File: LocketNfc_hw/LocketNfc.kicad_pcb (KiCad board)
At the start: 2 copper layers, 75.2 x 67.4 mm, 168 parts, among them M1 MOTOR_NO_CONTACTS, Q1 IRLML6401, Q2 IRLML6401, Q3 LED_RGB 5050, Q4 IRLML2030, SW1 SWITCH, SW2 IT1198, SW3 IT1198, SW4 IT1198

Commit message: Placement in progress
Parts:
- removed C123: 3.3pF, Capacitors:CAP_0402
- removed L123, L124: 12nH, Inductors:IND_0402
- removed TP2: TESTPOINT, PCB:TESTPOINT_1MM
- added C24: *, Capacitors:CAP_0402, B.Cu at (125.2, 85.7)
- added C59: 10u, Capacitors:CAP_0603_Silks, B.Cu at (195.0, 121.2)
- added C60: 10u, Capacitors:CAP_0603_Silks, B.Cu at (195.0, 118.4)
- added R29: 56k, Resistors:RES_0603, B.Cu at (185.2, 132.1)
- added R30: 56k, Resistors:RES_0603, B.Cu at (189.4, 132.1)
- added R31: 10k, Resistors:RES_0603, B.Cu at (190.9, 121.2)
- added R32: 10k, Resistors:RES_0603, B.Cu at (190.9, 118.4)
- ANT1: footprint Antennas:Locket5 -> Antennas:LocketNFC_inverted; moved to B.Cu
- C125: value 12pF -> 100pF; footprint Capacitors:CAP_0603 -> Capacitors:CAP_0402
- RP3, RP4, XL11, XL12: moved to F.Cu
- moved DD3 129.0 mm to (135.6, 83.8)
- moved C125 115.9 mm to (127.0, 84.0), turned to 0 degrees
- moved C121 113.1 mm to (129.6, 84.0), turned to 90 degrees
- moved L132 112.4 mm to (128.0, 85.2), turned to 0 degrees
- moved ANT1 112.0 mm to (124.1, 100.0), turned to 90 degrees
- moved C122 111.9 mm to (128.0, 82.8)
- moved C52 111.6 mm to (131.5, 86.8), turned to -90 degrees
- moved C51 110.2 mm to (131.5, 81.2), turned to 90 degrees
- moved L6 107.6 mm to (125.0, 84.0), turned to 0 degrees
- moved C49 104.5 mm to (133.5, 78.7), turned to 90 degrees
- moved XTAL3 102.4 mm to (135.5, 90.4)
- moved C28 95.4 mm to (135.8, 92.9)
- moved L131 91.1 mm to (131.2, 84.6), turned to 0 degrees
- moved XL11 90.2 mm to (135.3, 128.0), turned to 90 degrees
- moved XL12 90.0 mm to (132.4, 128.0), turned to 90 degrees
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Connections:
- C125 pad 2: /ANT0 -> /RF5
- DD1 pad 1: /AU_MCLK -> unconnected-(DD1-Pad1)
- DD1 pad 67: /AU_MCLK -> unconnected-(DD1-Pad67)
- MDL1 pad 10: /AU_MCLK -> /AU_LRCK
- MDL1 pad 11: /AU_LRCK -> /AU_BITCK
- MDL1 pad 12: /AU_BITCK -> /AU_SDA
- MDL1 pad 24: GND -> Net-(MDL1-Pad24)
- MDL1 pad 8: /AU_SDA -> /ESP_AUX
- MDL1 pad 9: /ESP_AUX -> unconnected-(MDL1-Pad9)
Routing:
- net VCC: track 0.00 -> 17.6 mm
- net +PwrMCU: track 0.00 -> 16.2 mm
- net GND: track 8.99 -> 20.3 mm
- net Net-(C1-Pad1): track 0.00 -> 10.4 mm
- net Net-(C15-Pad2): track 0.00 -> 4.74 mm
- net /RF3: track 0.00 -> 3.80 mm
- net /RF4: track 0.00 -> 3.75 mm
- net Net-(DD1-Pad13): track 0.00 -> 3.04 mm
- net /RF5: track 0.00 -> 2.50 mm
- net Net-(DD3-Pad17): track 0.00 -> 2.35 mm
- net Net-(C30-Pad2): track 0.00 -> 2.09 mm
- net /RF2: track 0.00 -> 2.04 mm
- net /RF1: track 0.00 -> 2.04 mm
- net Net-(C2-Pad1): track 0.00 -> 1.95 mm
- net /CC_MISO: track 0.00 -> 1.72 mm
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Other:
- copper layers 2 -> 4

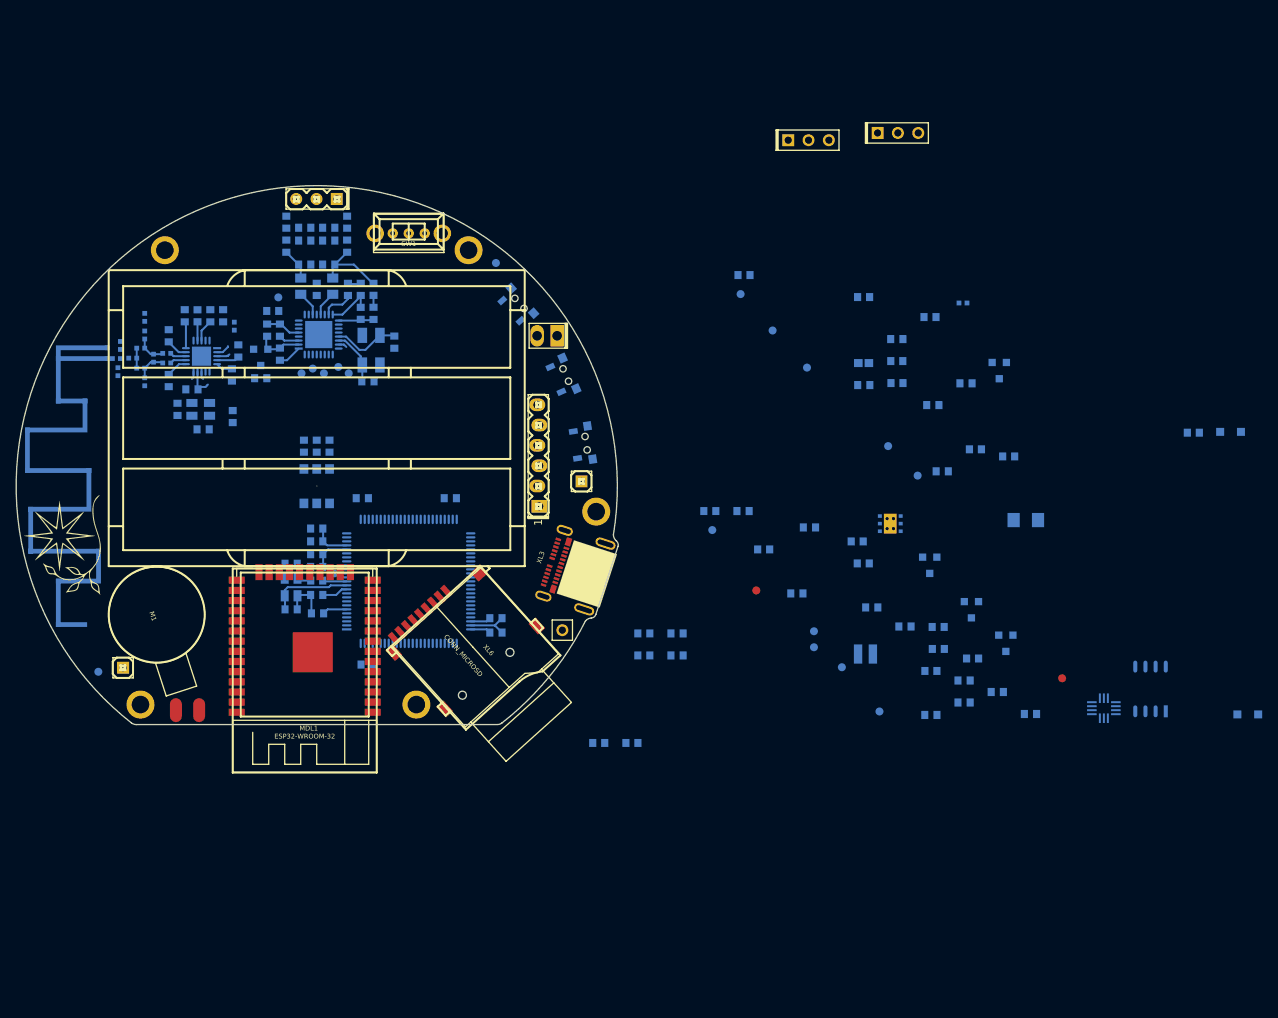
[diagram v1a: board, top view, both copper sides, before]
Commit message: Main PCB sent to factory
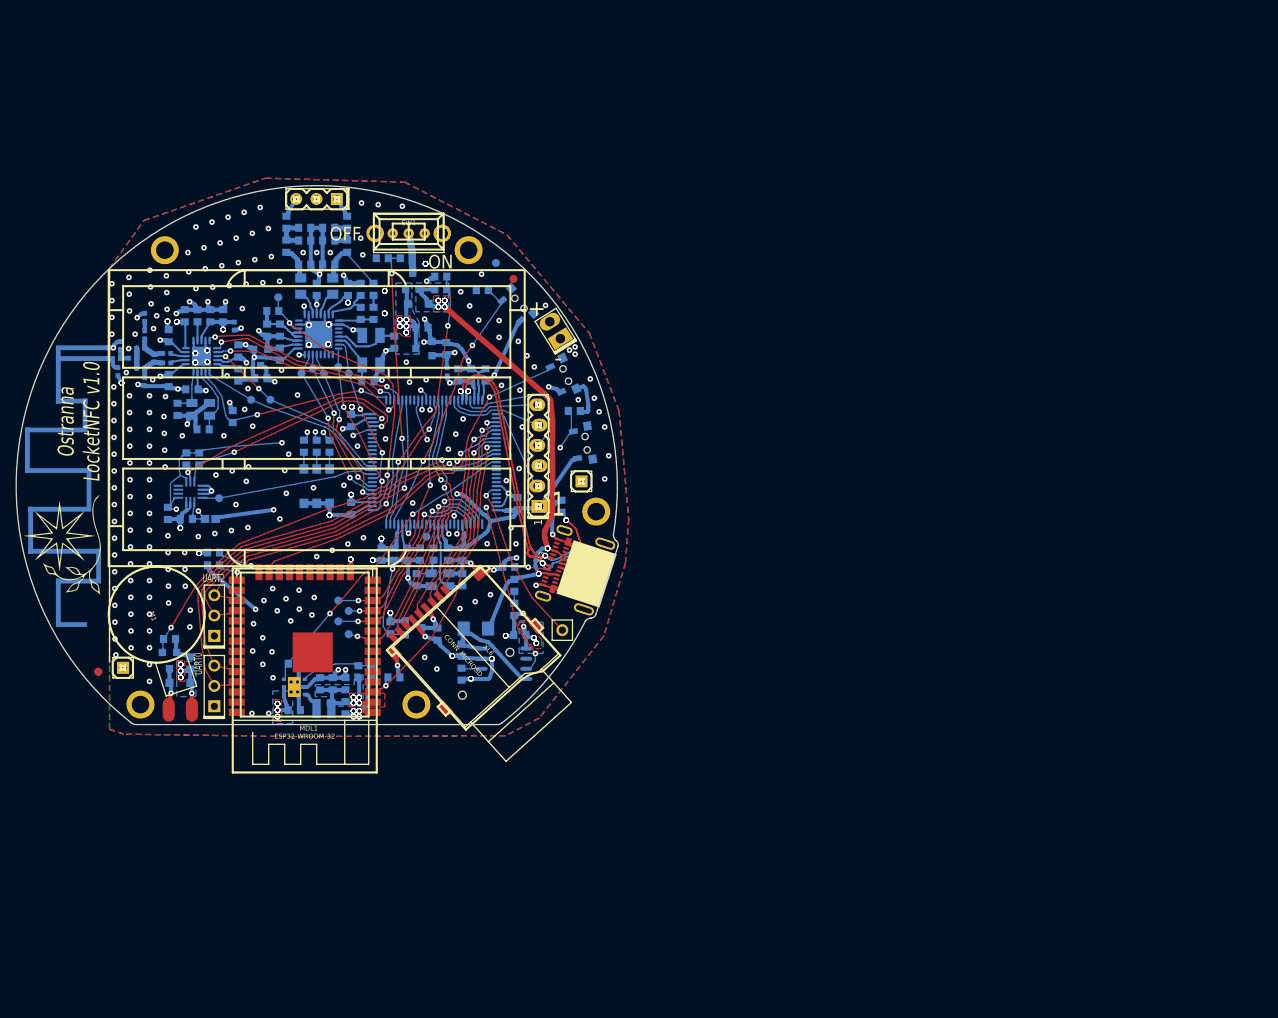
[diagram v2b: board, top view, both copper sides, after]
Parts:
- removed C59, C60: 10u, Capacitors:CAP_0603_Silks
- removed TP14, TP15, TP16: TESTPOINT, PCB:TESTPOINT_1MM
- R23: value 1k -> 68R
- R24: value 1k -> 330R
- R25: value 1k -> 150R
- moved D2 133.5 mm to (132.9, 124.6)
- moved RP3 120.5 mm to (122.7, 123.2)
- moved DD4 117.4 mm to (134.2, 100.7)
- moved XL4 109.6 mm to (137.2, 127.5), turned to 90 degrees
- moved D1 102.8 mm to (162.7, 77.2), turned to 0 degrees
- moved C56 98.2 mm to (134.2, 122.1), turned to -90 degrees
- moved R26 97.0 mm to (135.3, 96.6), turned to 90 degrees
- moved Q4 95.8 mm to (131.6, 121.8)
- moved XL5 94.8 mm to (137.2, 118.7), turned to 90 degrees
- moved C25 87.9 mm to (147.2, 128.0), turned to 0 degrees
- moved R27 87.0 mm to (133.7, 96.6), turned to 90 degrees
- moved R28 86.8 mm to (131.6, 119.1), turned to 0 degrees
- moved C47 85.7 mm to (153.6, 124.7), turned to 90 degrees
- moved F1 84.0 mm to (136.7, 104.1)
- moved TP17 83.9 mm to (137.8, 101.5)
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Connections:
- net /RF5 renamed /ANT0
- Q3 pad 1: GND -> Net-(Q3-Pad1)
- Q3 pad 2: GND -> Net-(Q3-Pad2)
- Q3 pad 3: GND -> Net-(Q3-Pad3)
- Q3 pad 4: Net-(Q3-Pad4) -> GND
- Q3 pad 5: Net-(Q3-Pad5) -> GND
- Q3 pad 6: Net-(Q3-Pad6) -> GND
- R23 pad 2: Net-(Q3-Pad4) -> Net-(Q3-Pad1)
- R24 pad 2: Net-(Q3-Pad5) -> Net-(Q3-Pad2)
- R25 pad 2: Net-(Q3-Pad6) -> Net-(Q3-Pad3)
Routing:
- net GND: track 20.3 -> 484.3 mm, vias 0 -> 370
- net +PwrMCU: track 16.2 -> 180.7 mm, vias 0 -> 25
- net +PwrUnst: track 0.00 -> 100.6 mm, vias 0 -> 57
- net /USB_D+: track 0.00 -> 73.8 mm, vias 0 -> 15
- net +BATT: track 0.00 -> 73.2 mm, vias 0 -> 11
- net /USB_D-: track 0.00 -> 67.3 mm, vias 0 -> 15
- net /+5V_USB: track 0.00 -> 63.7 mm, vias 0 -> 30
- net /ESP_TX0_MCU_RX: track 0.00 -> 58.4 mm, vias 0 -> 1
- net /ESP_RX0_MCU_TX: track 0.00 -> 54.5 mm, vias 0 -> 1
- net /Vibro_CTRL: track 0.00 -> 49.7 mm, vias 0 -> 2
- net /ESP_TX2_MCU_RX: track 0.00 -> 45.9 mm, vias 0 -> 1
- net /PWR_ACG: track 0.00 -> 43.7 mm, vias 0 -> 4
- net /ESP_RX2_MCU_TX: track 0.00 -> 41.2 mm, vias 0 -> 1
- net /ESP_GPIO0: track 0.00 -> 40.3 mm, vias 0 -> 2
- net /+PWR_ESP: track 0.00 -> 39.9 mm, vias 0 -> 21
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- added copper zone on B.Cu, net +BATT
- added copper zone on F.Cu, net +BATT
- added copper zone on In1.Cu, net +BATT
- added copper zone on In2.Cu, net +BATT
- added copper zone on B.Cu, net +PwrUnst
- added copper zone on F.Cu, net +PwrUnst
- added copper zone on In1.Cu, net +PwrUnst
- added copper zone on In2.Cu, net +PwrUnst
- added copper zone on B.Cu, net /+5V_USB
- added copper zone on F.Cu, net /+5V_USB
- added copper zone on In1.Cu, net /+5V_USB
- added copper zone on In2.Cu, net /+5V_USB
- added copper zone on B.Cu, net /+PWR_ESP
- added copper zone on F.Cu, net /+PWR_ESP
- added copper zone on In1.Cu, net /+PWR_ESP
- added copper zone on In2.Cu, net /+PWR_ESP
- added copper zone on B.Cu, net GND
- added copper zone on F.Cu, net GND
- added copper zone on In1.Cu, net GND
- added copper zone on In2.Cu, net GND
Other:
- outline, holes or cut-outs redrawn
- board text added: "+"
- board text added: "-"
- board text added: "1"
- board text added: "ACG"
- board text added: "AUX"
- board text added: "BCK"
- board text added: "Charger"
- board text added: "DBG"
- board text added: "GDO0"
- board text added: "GDO2"
- board text added: "GND"
- board text added: "IRQ"
- board text added: "LRCK"
- board text added: "MISO"
- board text added: "MOSI"
- board text added: "NSS"
- board text added: "OFF"
- board text added: "ON"
- board text added: "Ostranna LocketNFC v1.0"
- board text added: "RX0"
- board text added: "RX2"
- board text added: "SCK"
- board text added: "SDA"
- board text added: "Solder to power ACG always"
- board text added: "TX0"
- board text added: "TX2"
- board text added: "UART0"
- board text added: "UART2"
- board text added: "Vibro"

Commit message: Connects
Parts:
- turned Q3 to -90 degrees
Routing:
- net Net-(Q3-Pad3): track 0.00 -> 2.10 mm
- net GND: track 484.3 -> 482.2 mm
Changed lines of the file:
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@@
     )
   )
-  (footprint "LEDs:LED_5050" locked (layer "B.Cu")
-    (at 150 100 90)
+  (footprint "LEDs:LED_5050" (layer "B.Cu")
+    (at 150 100 -90)
     (property "Price" "7")
     (property "Sheetfile" "LocketNfc.kicad_sch")
@@
     (fp_line (start -2.49936 2.49936) (end 2.49936 2.49936) (layer "B.SilkS") (width 0.14986))
     (fp_circle (center 0 0) (end 0 -2.19964) (layer "B.SilkS") (width 0.14986) (fill none))
-    (pad "1" smd rect locked (at -2.15 1.6 90) (size 1.2 1.1) (layers "B.Cu" "B.Paste" "B.Mask")
+    (pad "1" smd rect locked (at -2.15 1.6 270) (size 1.2 1.1) (layers "B.Cu" "B.Paste" "B.Mask")
       (net 155 "Net-(Q3-Pad1)") (pintype "passive"))
-    (pad "2" smd rect locked (at -2.15 0 90) (size 1.2 1.1) (layers "B.Cu" "B.Paste" "B.Mask")
+    (pad "2" smd rect locked (at -2.15 0 270) (size 1.2 1.1) (layers "B.Cu" "B.Paste" "B.Mask")
       (net 156 "Net-(Q3-Pad2)") (pintype "passive"))
-    (pad "3" smd rect locked (at -2.15 -1.6 90) (size 1.2 1.1) (layers "B.Cu" "B.Paste" "B.Mask")
+    (pad "3" smd rect locked (at -2.15 -1.6 270) (size 1.2 1.1) (layers "B.Cu" "B.Paste" "B.Mask")
       (net 157 "Net-(Q3-Pad3)") (pintype "passive"))
-    (pad "4" smd rect locked (at 2.15 -1.6 90) (size 1.2 1.1) (layers "B.Cu" "B.Paste" "B.Mask")
+    (pad "4" smd rect locked (at 2.15 -1.6 270) (size 1.2 1.1) (layers "B.Cu" "B.Paste" "B.Mask")
       (net 2 "GND") (pinfunction "B") (pintype "passive"))
-    (pad "5" smd rect locked (at 2.15 0 90) (size 1.2 1.1) (layers "B.Cu" "B.Paste" "B.Mask")
+    (pad "5" smd rect locked (at 2.15 0 270) (size 1.2 1.1) (layers "B.Cu" "B.Paste" "B.Mask")
       (net 2 "GND") (pinfunction "G") (pintype "passive"))
-    (pad "6" smd rect locked (at 2.15 1.6 90) (size 1.2 1.1) (layers "B.Cu" "B.Paste" "B.Mask")
+    (pad "6" smd rect locked (at 2.15 1.6 270) (size 1.2 1.1) (layers "B.Cu" "B.Paste" "B.Mask")
       (net 2 "GND") (pintype "passive"))
     (model "${KICAD_SYMBOL_DIR}/3d/LED/LED_5050old.STEP"
@@
   (segment (start 132.9486 104.358) (end 132.9486 104.608) (width 0.5) (layer "B.Cu") (net 2))
   (segment (start 133.8761 102.9751) (end 133.7651 103.0001) (width 0.25) (layer "B.Cu") (net 2))
-  (segment (start 151.6 96.125) (end 151.6 95.75) (width 0.15) (layer "B.Cu") (net 2))
   (segment (start 124.5889 82.6983) (end 124.63 82.6195) (width 0.5) (layer "B.Cu") (net 2))
   (segment (start 153.6027 123.7435) (end 153.6027 123.4935) (width 0.5) (layer "B.Cu") (net 2))
@@
   (segment (start 166.708 82.2325) (end 166.458 82.2325) (width 0.5) (layer "B.Cu") (net 2))
   (segment (start 161.8884 112.2675) (end 161.742 112.1211) (width 0.5) (layer "B.Cu") (net 2))
-  (segment (start 151.6 97.25) (end 151.6 96.2) (width 0.15) (layer "B.Cu") (net 2))
   (segment (start 142.0435 85.992) (end 142.0435 85.8884) (width 0.5) (layer "B.Cu") (net 2))
   (segment (start 167.942 109.262) (end 168.2 109.262) (width 0.5) (layer "B.Cu") (net 2))
@@
   (segment (start 157.842 109.2498) (end 157.592 109.2498) (width 0.5) (layer "B.Cu") (net 2))
   (segment (start 147.198 82.8145) (end 147.25 82.8) (width 0.25) (layer "B.Cu") (net 2))
-  (segment (start 151.6 96.2) (end 151.6 96.125) (width 0.15) (layer "B.Cu") (net 2))
   (segment (start 142.0566 84.2574) (end 142.1944 83.8916) (width 0.5) (layer "B.Cu") (net 2))
   (segment (start 174.669 116.3565) (end 174.7 116.162) (width 0.5) (layer "B.Cu") (net 2))
@@
   (segment (start 183.4 90.725) (end 183.15 90.725) (width 0.5) (layer "B.Cu") (net 2))
   (segment (start 150.142 124.1325) (end 150.4 123.938) (width 0.5) (layer "B.Cu") (net 2))
-  (segment (start 151.6 97.325) (end 151.6 97.25) (width 0.15) (layer "B.Cu") (net 2))
   (segment (start 160.2 123.4) (end 160.2 123.65) (width 0.5) (layer "B.Cu") (net 2))
   (segment (start 138.558 77.4935) (end 138.558 77.3899) (width 0.5) (layer "B.Cu") (net 2))
@@
   (segment (start 131.242 87.5) (end 130.992 87.5) (width 0.5) (layer "B.Cu") (net 2))
   (segment (start 154.158 74.638) (end 153.9 74.638) (width 0.5) (layer "B.Cu") (net 2))
-  (segment (start 151.6 97.85) (end 151.6 97.325) (width 0.15) (layer "B.Cu") (net 2))
   (segment (start 131.908 104.131) (end 131.658 104.131) (width 0.5) (layer "B.Cu") (net 2))
   (segment (start 153.642 74.1935) (end 153.642 74.0899) (width 0.5) (layer "B.Cu") (net 2))
@@
   (segment (start 150 97.85) (end 150 97.325) (width 0.15) (layer "B.Cu") (net 156))
   (segment (start 150 96.125) (end 150 95.75) (width 0.15) (layer "B.Cu") (net 156))
+  (segment (start 151.6 96.125) (end 151.6 95.75) (width 0.15) (layer "B.Cu") (net 157))
+  (segment (start 151.6 97.25) (end 151.6 96.2) (width 0.15) (layer "B.Cu") (net 157))
+  (segment (start 151.6 96.2) (end 151.6 96.125) (width 0.15) (layer "B.Cu") (net 157))
+  (segment (start 151.6 97.325) (end 151.6 97.25) (width 0.15) (layer "B.Cu") (net 157))
+  (segment (start 151.6 97.85) (end 151.6 97.325) (width 0.15) (layer "B.Cu") (net 157))
   (segment (start 178.0266 110.2924) (end 177.965 110.2925) (width 0.15) (layer "F.Cu") (net 158))
   (segment (start 178.9683 110.4595) (end 178.6883 110.4315) (width 0.15) (layer "F.Cu") (net 158))
